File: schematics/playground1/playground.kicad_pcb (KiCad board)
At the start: 2 copper layers, 92.5 x 88 mm, 98 parts, among them J1 Conn_01x05, J2 Conn_02x03_Odd_Even, J3 Conn_01x03, J4 Conn_02x04_Odd_Even, SW1 SW_SPST, SW2 SW_Push, SW3 SW_Push, U1 ADS1299, U2 MCP1700x-330xxTT, U3 PIC32MX250F128B_I_SS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

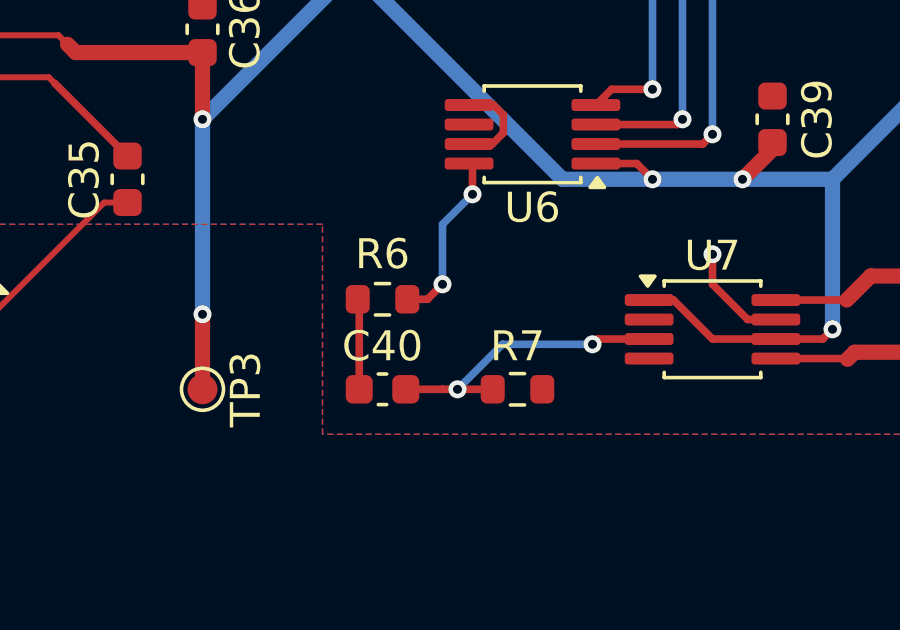
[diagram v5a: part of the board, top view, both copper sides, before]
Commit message: traced pcb audio subsys edits
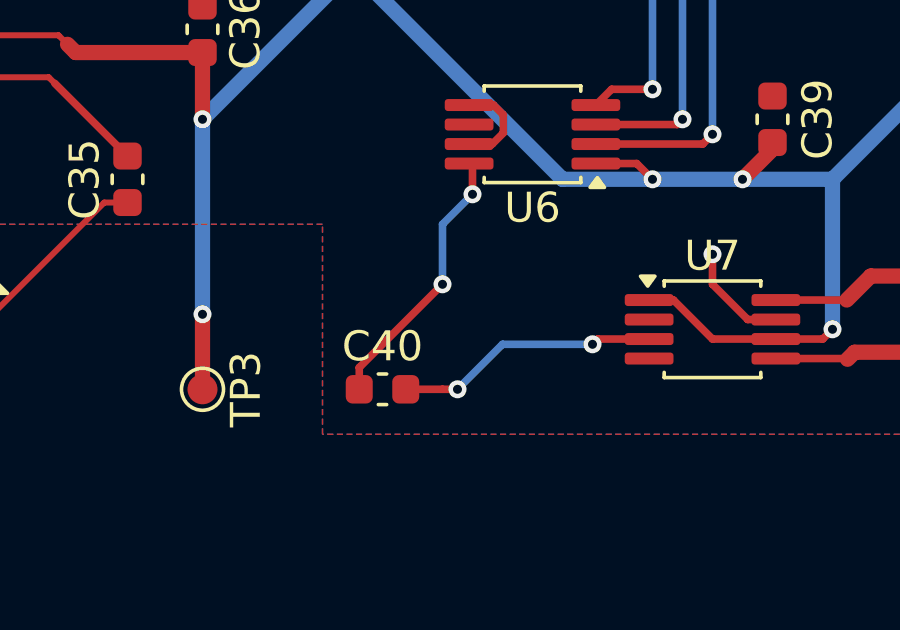
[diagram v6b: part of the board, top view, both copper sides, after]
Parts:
- removed R6: 1k, Resistor_SMD:R_0603_1608Metric
- removed R7: 100k, Resistor_SMD:R_0603_1608Metric
- C40: value 1uF -> 0.1uF
- U4: footprint ble_footprints:Raytac_MDBT42Q -> RF_Module:Raytac_MDBT42Q
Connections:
- C40 pad 1: Net-(C40-Pad1) -> Net-(U6-VA)
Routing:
- net Net-(U6-VA): track 5.87 -> 9.14 mm
- net Net-(C40-Pad1): track 3.02 -> 0.00 mm
- net Net-(U7-IN+): track 9.98 -> 8.81 mm

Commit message: resolve changes
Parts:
- U4: footprint RF_Module:Raytac_MDBT42Q -> ble_footprints:Raytac_MDBT42Q
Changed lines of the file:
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@@
 		)
 	)
-	(footprint "RF_Module:Raytac_MDBT42Q"
+	(footprint "ble_footprints:Raytac_MDBT42Q"
 		(layer "F.Cu")
 		(at 143.4 136.7 180)
@@
 			)
 		)
-		(property "Datasheet" "https://www.raytac.com/download/index.php?index_id=27"
+		(property "Datasheet" ""
 			(at 0 0 180)
 			(unlocked yes)
@@
 			)
 		)
-		(property "Description" "Multiprotocol BLE/ANT/2.4 GHz/802.15.4 Cortex-M4F SoC, nRF52832 module, ceramic antenna"
+		(property "Description" ""
 			(at 0 0 180)
 			(unlocked yes)
@@
 			)
 		)
-		(fp_text_box "KEEP-OUT AREA"
-			(start -6 -9)
-			(end 6 -4.2)
+		(fp_text_box "No Ground-Pad Area"
+			(start -0.5 -4.2)
+			(end 3.9 -1.1)
 			(margins 0.35 0.35 0.35 0.35)
 			(layer "Dwgs.User")
@@
 			)
 		)
-		(fp_text_box "No Ground-Pad Area"
-			(start -0.5 -4.2)
-			(end 3.9 -1.1)
+		(fp_text_box "KEEP-OUT AREA"
+			(start -6 -9)
+			(end 6 -4.2)
 			(margins 0.35 0.35 0.35 0.35)
 			(layer "Dwgs.User")
@@
 				(tracks not_allowed)
 				(vias not_allowed)
-				(pads not_allowed)
+				(pads allowed)
 				(copperpour not_allowed)
 				(footprints not_allowed)
@@
 			(keep_text_aligned yes)
 		)
-		(gr_text "3169.2913"
+		(gr_text "80.5"
 			(at 196.35 110.25 90)
 			(layer "Dwgs.User")
@@
 			(keep_text_aligned yes)
 		)
-		(gr_text "3326.7717"
+		(gr_text "84.5"
 			(at 138.25 54.35 0)
 			(layer "Dwgs.User")
@@
 			(keep_text_aligned yes)
 		)
-		(gr_text "3169.2913"
+		(gr_text "80.5"
 			(at 77.85 110.25 90)
 			(layer "Dwgs.User")
@@
 			(keep_text_aligned yes)
 		)
-		(gr_text "3326.7717"
+		(gr_text "84.5"
 			(at 138.25 160.35 0)
 			(layer "Dwgs.User")
